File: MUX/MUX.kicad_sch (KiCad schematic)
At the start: 103 parts, among them P1 Conn_02x36_Top_Bottom, P2 DB9_Male, P3 DB9_Male, P4 DB9_Male, P5 DB9_Male

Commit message: WIP cards
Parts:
- added R16: 1K, symbol Device:R
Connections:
- net ~{ReadInput} is gone; now on net GND: U_B5.1 (OEa), U_B5.15 (OEb)
- net +5V: now also U_B2.14 (V_{CC}), R16.2; no longer U_B2.1 (V_{CC})
- net Data.InBD_{1}: now also U_H1.38 (CLS_{1}), U_H2.38 (CLS_{1}), U_H3.38 (CLS_{1})
- net GND: now also U_B2.7 (GND), U_C1.2 (Ia<b), U_C1.4 (Ia>b), U_C2.2 (Ia<b), U_C2.4 (Ia>b), U_C7.10 (CET), U_C7.9 (~{PE}); no longer U_B2.8 (GND)
- net ~{Reset}: now also U_C8.13
- net Write: now reaches U_B4.4, U_D2.12
- net Write: now also U_D1.2
- net INT_Pending: now reaches U_B7.9, U_E7.11
- net INT_Pending: now also U_B7.5
- net SysA_{3}: now reaches U_A1.12, U_B1.12, U_D1.3, U_D1.4, U_D1.5, U_E4.20 (A3)
- net ~{INT_Request}: now reaches U_A3.10, U_A7.10, U_B7.6, U_D8.2 (D)
- net INT_Request: now reaches U_A3.4, U_A7.5, U_A7.8, U_B7.1
- net ForceTXEInt: now reaches U_C6.10, U_C6.4, U_D3.8, U_E7.1, U_E7.4
- net ~{SysDataOutEN}: now reaches U_A5.9 (OE), U_A6.9 (OE), U_A8.8
- net ~{DirectRead}: now reaches U_C6.2, U_D1.8, U_E2.12 (A3)
- net at U_C6.3: now also U_A8.9; no longer U_D8.1 (~{R})
- net INR_OUT: now reaches U_A4.10, U_A4.13, U_A4.2, U_A4.4, U_A7.3
- net ~{INT_INH}: now reaches U_B7.10
- net ~{INT_INH}: now also U_A3.9, U_A8.12, U_B7.4
- net LevelAllow: now reaches U_B7.13
- net LevelAllow: now also U_A3.5, U_B3.7 (Oa<b)
- net at U_C8.4, U_D8.5 (Q): now also U_C8.1
- net MUX3.RxD: now reaches U_F4.2 (I1), U_F5.8, U_F6.7 (D3)
- net Read: now reaches U_B4.2, U_D2.11, U_D3.3
- net Read: now also U_D1.9
- net at U_D2.13: now also U_D2.2
- net DirectAddressed: now reaches U_C1.6 (Oa=b), U_D1.1, U_D3.1
- net DirectAddressed: now also U_D1.11
- net ~{DirectAddressed}: now reaches U_D3.2
- net ~{DirectAddressed}: now also U_B6.1, U_D2.3
- net Phase3: now reaches U_C7.12 (Q2)
- net Phase3: now also U_D2.9
- net Phase2: now reaches U_C7.13 (Q1)
- net Phase2: now also U_C7.5 (D2)
- net Phase1: now reaches U_C7.14 (Q0), U_D1.13, U_J7.1
- net Phase1: now also U_C7.4 (D1)
- net at U_C7.3 (D0), U_C7.6 (D3): now also U_D8.1 (~{R}), R16.1
- net CommonRead: now reaches U_D2.4
- net CommonRead: now also U_D2.8, U_D3.5
- net ~{SelfReset}: now reaches U_A7.12, U_B6.13, U_B8.8 (~{Q})
- net ~{DirectWrite}: now reaches U_D1.12, U_E4.18 (E0), U_E4.19 (E1)
- net D4_1 renamed ~{CommonRead}
- net RTS_EN renamed RTS_REG_EN
- net ~{is_common_addressed} renamed ~{CommonAddressed}
- no-connect marks 82 -> 136
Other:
- note added: "(~{Reset})"
- note added: "(~{Set})"
- note added: "MUX0"
- note added: "Status registers only output 6 bits this drives the other 2 high bits to 0 (see U_D4)"
- note added: "The shift function isn't even used. lul This register holds the value for the custom baud rate select."
- note added: "This counter pair provides a divide-by-N Loading the register will reset both counters so do not change while send or receive is in progress These count UP so the formula will be: Baud = MaxBaud / (256 - N) N must be less than 255 or it will not count *MaxBaud = Crystal / 256"
- note added: "U_B2B matches the high nibble including ~{A_{15}} which on the CPU6, places the device in the 0x3Fnnn memory range for older buses, it's just 0xFnnn"
- note added: "congradulations! it's a shift register with reset! This provides the read/write cycle phases phase 1 is used to fetch data during write phase 3 will assert ~{DRDY} at cycle end"
- note added: "low register"
- note removed: "(via)"
- note removed: "15 or 14? (needs lookup)"
- note removed: "C7(input) to D2.9 (via)"
- note removed: "D2.8/D3.5(via)"
- note removed: "MUX4"
- note removed: "TODO"
- note removed: "The shift function isn't even used. lul"
- note removed: "This matches the high nibble including ~{A_{15}} which on the CPU6, places the device in the 0x3Fnnn memory range for older buses, it's just 0xFnnn"
- note removed: "addressed"
- note removed: "addressed (via)"
- note removed: "is read"
- note removed: "not high reg probably pin 10"
- note removed: "not write"
- note removed: "read"
- note removed: "to reset?"
- note removed: "what even is this thing? is it right?"
- note removed: "write"
- note removed: "~{is addressed}"
- note removed: "~{read}"
- moved on the sheet: P2, P3, P4, P5, R1, R10, R13, R15, R2, R3, R4, R5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

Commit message: finished MUX
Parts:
- U_B2: symbol 74xx:SN7425 -> 74xx_legacy:SN7425
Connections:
- net RTS4_TTL is gone; now on net RTS3_TTL: U_K8.7 (Q3), U_LL8.3
- net RTS1_TTL: now also U_K8.5 (Q1), U_L8.3; no longer U_K8.4 (Q0), U_L8.2
- net RTS2_TTL: now also U_K8.6 (Q2), U_LL8.2; no longer U_K8.5 (Q1), U_L8.3
- net RTS3_TTL: no longer U_K8.6 (Q2), U_LL8.2
- net TX_{2}_TTL: now reaches U_K6.10, U_L6.3
- net ~{TX_{2}_EIA}: now reaches P4.7, U_K6.11, U_K6.12
- net SysA_{2}: now reaches U_A1.6, U_B1.1, U_E2.13 (A2), U_E4.21 (A2)
- net CausePending: now reaches U_B1.11, U_B8.4 (~{S}), U_D8.6 (~{Q})
- net SysA_{1}: now reaches U_A1.4, U_B1.2, U_B1.4, U_E2.14 (A1), U_E4.22 (A1)
- net SysA_{0}: now reaches U_A1.2, U_B1.3, U_E2.15 (A0), U_E4.23 (A0)
- net MMIO_HSel: now reaches U_B1.5, U_C1.3 (Ia=b), U_C2.6 (Oa=b)
- net CTS_{1}_TTL: now reaches U_F2.10 (I4), U_K6.2
- net LoadCR_{0}: now reaches U_E5.2, U_H1.34 (CRL), U_L1.13 (E01), U_L1.4 (E23)
- net TxBE_{3}: now reaches U_E3.11, U_E6.3 (C), U_F4.14 (I6)
- net RxD_{2}: now reaches U_F3.2 (I1), U_F5.6, U_F6.6 (D2)
- net TX_{2}_OUT: now reaches U_H3.25 (TxOUT), U_K6.13
- net ~{RTS_{3}}: now reaches P5.4, U_LL8.6
- net ~{RTS_{2}}: now reaches P4.4, U_LL8.7
- net LoadCR_{1}: now reaches U_E5.4, U_H2.34 (CRL), U_L2.13 (E01), U_L2.4 (E23)
- net ~{ReadSR_{0}}: now reaches U_E1.13, U_E2.1 (0), U_F1.1 (OEa), U_F1.15 (OEb)
- net ~{ReadRxB_{0}}: now reaches U_E2.2 (1), U_H1.18 (~{RxDR}), U_H1.4 (~{RxB_OE})
- net ~{ReadSR_{1}}: now reaches U_E1.12, U_E2.3 (2), U_F2.1 (OEa), U_F2.15 (OEb)
- net ~{ReadRxB_{1}: now reaches U_E2.4 (3), U_H2.18 (~{RxDR}), U_H2.4 (~{RxB_OE})
- net ~{ReadSR_{2}}: now reaches U_E1.10, U_E2.5 (4), U_F3.1 (OEa), U_F3.15 (OEb)
- net ~{ReadRxB_{2}}: now reaches U_E2.6 (5), U_H3.18 (~{RxDR}), U_H3.4 (~{RxB_OE})
- net ~{ReadSR_{3}: now reaches U_E1.9, U_E2.7 (6), U_F4.1 (OEa), U_F4.15 (OEb)
- net ~{ReadRxB_{3}}: now reaches U_E2.9 (7), U_H4.18 (~{RxDR}), U_H4.4 (~{RxB_OE})
- net ~{INTHandled}: now reaches U_C8.1, U_C8.4, U_D8.5 (Q)
- net RX_{3}_IN: now reaches U_H4.20 (RxIN), U_L7.10 (4Y)
- net RX_{2}_IN: now reaches U_H3.20 (RxIN), U_L7.12 (2Y)
- net ~{CTS_{2}}: now reaches P4.2, U_L7.4 (1A)
- net ~{RX_{2}}: now reaches P4.8, U_L7.5 (2A)
- net ~{CTS_{3}}: now reaches P5.2, U_L7.6 (3A)
- net ~{RX_{3}}: now reaches P5.8, U_L7.7 (4A)
- net CTS_{3}_TTL: now reaches U_F4.10 (I4), U_J6.2
- net FrameF_{3}: now reaches U_F4.12 (I5), U_H4.14 (FError)
- net ParityF_{3}: now reaches U_F4.4 (I2), U_H4.13 (PError)
- net OverrunF_{3}: now reaches U_F4.6 (I3), U_H4.15 (OError)
- net LoadCR_{2}: now reaches U_E5.6, U_H3.34 (CRL), U_L3.13 (E01), U_L3.4 (E23)
- net TxBE_{1}: now reaches U_D6.11 (C), U_E3.6, U_F2.14 (I6)
- net TX_{1}_TTL: now reaches U_K6.4, U_LL6.3
- net ~{TX_{1}}: now reaches P3.6, U_LL6.6
- net TX_{3}_OUT: now reaches U_H4.25 (TxOUT), U_J5.13
- net LoadCR_{3}: now reaches U_E5.10, U_H4.34 (CRL), U_L4.13 (E01), U_L4.4 (E23)
- net ~{CauseHold}: now reaches U_E7.8, U_F6.13 (E01), U_F6.4 (E23), U_F7.13 (E01), U_F7.4 (E23)
- net TX_{3}_TTL: now reaches U_J5.4, U_L6.2
- net ~{TX_{2}}: now reaches P4.6, U_L6.6
- net ~{TX_{3}}: now reaches P5.6, U_L6.7
- net CTS_{2}_TTL: now reaches U_F3.10 (I4), U_J6.12
- net ParityF_{1}: now reaches U_F2.4 (I2), U_H2.13 (PError)
- net FrameF_{1}: now reaches U_H2.14 (FError)
- net FrameF_{1}: now also U_F2.12 (I5)
- net OverrunF_{1}: now reaches U_H2.15 (OError)
- net OverrunF_{1}: now also U_F2.6 (I3)
- net RX_{1}_IN: now reaches U_H2.20 (RxIN), U_L5.10 (4Y)
- net TX_{1}_OUT: now reaches U_H2.25 (TxOUT), U_J6.3
- net ~{CREndStrobe}: now reaches U_B8.5 (Q), U_C8.12
- net ~{TX_{3}_EIA}: now reaches P5.7, U_J5.12, U_J5.3
- net ParityF_{2}: now reaches U_F3.4 (I2), U_H3.13 (PError)
- net FrameF_{2}: now reaches U_F3.12 (I5), U_H3.14 (FError)
- net OverrunF_{2}: now reaches U_F3.6 (I3), U_H3.15 (OError)
- net ~{CTS_{1}}: now reaches P3.2, U_L5.6 (3A)
- net ~{TX_{1}_EIA}: now reaches P3.7, U_J6.4, U_K6.3
- net ~{RX_{1}}: now reaches P3.8, U_L5.7 (4A)
- net CTS_{0}_TTL: now reaches U_F1.10 (I4), U_J5.10
- net FrameF_{0}: now reaches U_F1.12 (I5), U_H1.14 (FError)
- net TxBE_{0}: now reaches U_D6.3 (C), U_E3.3, U_F1.14 (I6)
- net ParityF_{0}: now reaches U_F1.4 (I2), U_H1.13 (PError)
- net OverrunF_{0}: now reaches U_F1.6 (I3), U_H1.15 (OError)
- net LoadIPL: now reaches U_C5.10 (CP), U_D3.12
- net RX_{0}_IN: now reaches U_H1.20 (RxIN), U_L5.12 (2Y)
- net TxBE_{2}: now reaches U_E3.8, U_E6.11 (C), U_F3.14 (I6)
- net CTS1 renamed ~{CTS_{0}}
- net F6_D0 renamed RxD_{0}
- net F6_D1 renamed RxD_{1}
- net MUX3.RxD renamed RxD_{3}
- net RTS1 renamed ~{RTS_{0}}
- net RTS2 renamed ~{RTS_{1}}
- net RTS_REG_EN renamed ~{RTS_REG_EN}
- net RXD1 renamed ~{RX_{0}}
- net TXD1 renamed ~{TX_{0}}
- net TXD1_BUF renamed TX_{0}_TTL
- net TXD1_TTL renamed TX_{0}_OUT
- net ~{CBRL} renamed ~{LoadCBR}
- net ~{CRL1} renamed ~{LoadCR_{0}}
- net ~{CRL2} renamed ~{LoadCR_{1}}
- net ~{CRL3} renamed ~{LoadCR_{2}}
- net ~{CRL4} renamed ~{LoadCR_{3}}
- net ~{IPLL} renamed ~{LoadIPL}
- net ~{RTSL} renamed ~{LoadRTS}
- net ~{TXBL1} renamed ~{LoadTxB_{0}}
- net ~{TXBL2} renamed ~{LoadTxB_{1}}
- net ~{TXBL3} renamed ~{LoadTxB_{2}}
- net ~{TXBL4} renamed ~{LoadTxB_{3}}
- net ~{TXD1_TTL} renamed ~{TX_{0}_EIA}
- new net RTS0_TTL: U_K8.4 (Q0), U_L8.2
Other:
- note added: "(-12V)"
- note added: "(GND)"
- note added: "*^{1} Reading this register is only valid during an interrupt"
- note added: "*^{2} Baud = Crystal / (256 * (256 - N)); N != 0"
- note added: "1.5"
- note added: "1200"
- note added: "19200"
- note added: "2400"
- note added: "300"
- note added: "4"
- note added: "4800"
- note added: "4915200 MHz"
- note added: "5"
- note added: "6"
- note added: "7"
- note added: "75"
- note added: "8"
- note added: "9"
- note added: "9600"
- note added: "A"
- note added: "B"
- note added: "Baud"
- note added: "Baud Rate Gen Divide *^{2}"
- note added: "Baud Rate Select"
- note added: "C"
- note added: "CTS"
- note added: "Card Address"
- note added: "Card Number"
- note added: "Clear to Send (pin 2)"
- note added: "Control Bits"
- note added: "D"
- note added: "D8A when set, will always set B8A"
- note added: "Data"
- note added: "Data Bits Length"
- note added: "E"
- note added: "Even"
- note added: "F"
- note added: "F20F *^{1}"
- note added: "Force TXE MUX 3..0"
- note added: "FrEr"
- note added: "Framing Error"
- note added: "Interrupt Cause MMIO bits (0xF20F Read)"
- note added: "Interrupts Off (Any write)"
- note added: "Interrupts On (Any write)"
- note added: "Length Select"
- note added: "MUX 0"
- note added: "MUX 1"
- note added: "MUX 2"
- note added: "MUX 3"
- note added: "MUX Card Reset (Any write)"
- note added: "N"
- note added: "N / 16"
- note added: "N / 2"
- note added: "N / 256"
- note added: "N / 4"
- note added: "N / 64"
- note added: "N / 8"
- note added: "N/A"
- note added: "OvRE"
- note added: "PDis"
- note added: "PEr"
- note added: "Parity 0=Enable, 1=Disable"
- note added: "Parity 0=Odd, 1=Even"
- note added: "Parity Mismatch Error"
- note added: "Q follows D when Enabled (H)"
- note added: "Rate Gen"
- note added: "Read"
- note added: "Receive Data Available"
- note added: "Receive Overrun"
- note added: "Reg"
- note added: "Rx Data"
- note added: "RxDi"
- note added: "Set IPL"
- note added: "Status Bits"
- note added: "Stop"
- note added: "Stop Bits Length"
- note added: "The shift function isn't even used. lul This register holds the value for the custom baud rate select. a 74LS273 might have been a better option"
- note added: "This counter pair provides a divide-by-N Loading the register will reset both counters this skews the output, so do not change while send or receive is in progress These count UP so the formula will be: Baud = MaxBaud / (256 - N) N must be less than 255 or it will not count *MaxBaud = Crystal / 256"
- note added: "Transmit Buffer Empty"
- note added: "Tx Data"
- note added: "TxEm"
- note added: "Write"
- note added: "fanout is at most 12 did they assume that the 8835 can't drive that?"
- note added: "it's a shift register with reset! This provides the read/write cycle phases phase 1 is used to fetch data during write phase 3 will assert ~{DRDY} at cycle end"
- note added: "this nand will go low when 0xF20F is accessed AND this device dispatched an interrupt"
- note removed: "A0"
- note removed: "A1"
- note removed: "A2"
- note removed: "A3"
- note removed: "E8"
- note removed: "E8 Func"
- note removed: "EN"
- note removed: "F8"
- note removed: "F8 Func"
- note removed: "I/O bits"
- note removed: "S0"
- note removed: "S1"
- note removed: "S2"
- note removed: "The shift function isn't even used. lul This register holds the value for the custom baud rate select."
- note removed: "This counter pair provides a divide-by-N Loading the register will reset both counters so do not change while send or receive is in progress These count UP so the formula will be: Baud = MaxBaud / (256 - N) N must be less than 255 or it will not count *MaxBaud = Crystal / 256"
- note removed: "congradulations! it's a shift register with reset! This provides the read/write cycle phases phase 1 is used to fetch data during write phase 3 will assert ~{DRDY} at cycle end"
- note removed: "ok"
- note removed: "ok via"
- note removed: "should connect data out? enable?"
- note removed: "should connect to buffer input"
- note removed: "this nand will go low when 0xF20F is accessed AND this device is interrupting AND interrupts are not preempted"
- note removed: "~{D5_En}"
- moved on the sheet: JP1, JP2, JP3, JP4, P2, P3, P4, P5, R1, R10, R11, R12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

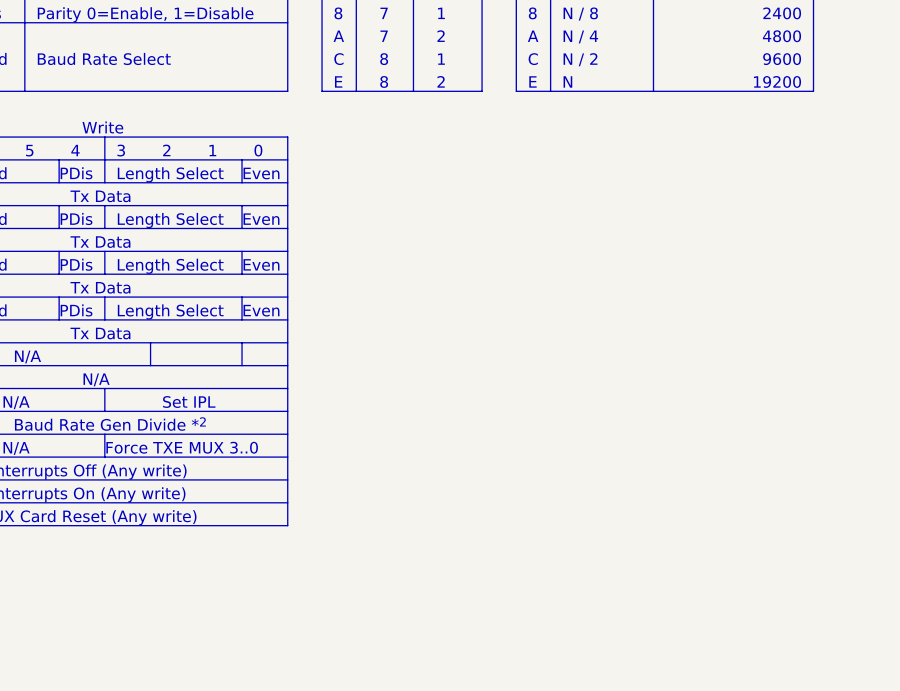
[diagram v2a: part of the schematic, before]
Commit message: MUX table, CPU net labels, partial DSK
MUX register table was missing description of RTS
Some internal nets in CPU were renamed to better describe them
DSK1 draft + DSK2 wip added
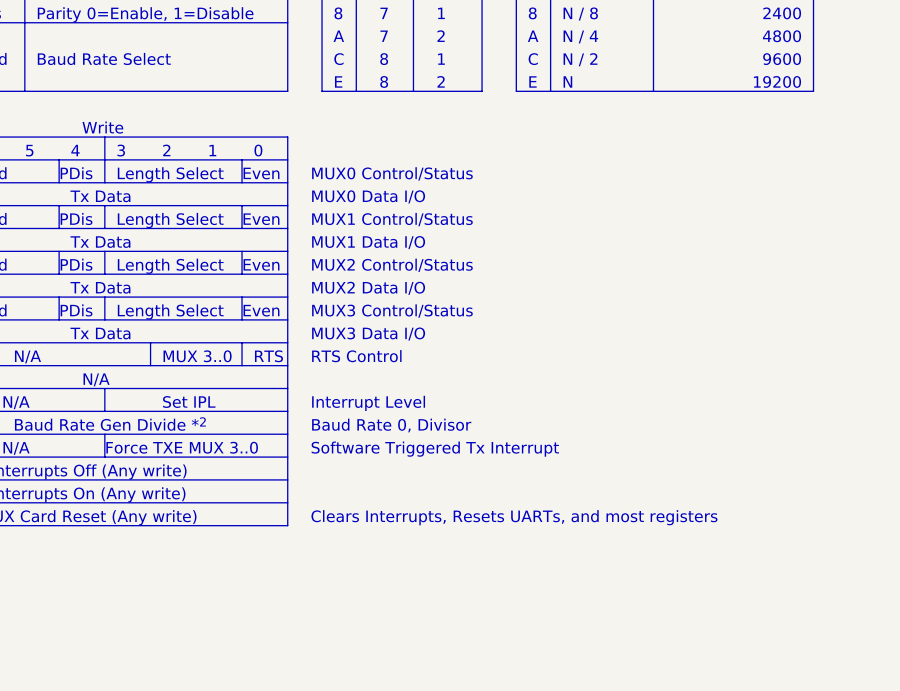
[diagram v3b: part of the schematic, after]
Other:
- note added: "Baud Rate 0, Divisor"
- note added: "Clears Interrupts, Resets UARTs, and most registers"
- note added: "Interrupt Level"
- note added: "MUX 3..0"
- note added: "MUX0 Control/Status"
- note added: "MUX0 Data I/O"
- note added: "MUX1 Control/Status"
- note added: "MUX1 Data I/O"
- note added: "MUX2 Control/Status"
- note added: "MUX2 Data I/O"
- note added: "MUX3 Control/Status"
- note added: "MUX3 Data I/O"
- note added: "RTS"
- note added: "RTS Control"
- note added: "Software Triggered Tx Interrupt"
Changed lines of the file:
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@@
     (stroke (width 0) (type default) (color 0 0 0 0))
   )
+  (text "MUX1 Data I/O" (at 948.69 435.61 0)
+    (effects (font (size 1.27 1.27)) (justify left bottom))
+  )
   (text "F" (at 902.97 466.09 0)
     (effects (font (size 1.27 1.27)) (justify left bottom))
@@
     (effects (font (size 1.27 1.27)) (justify left bottom))
   )
+  (text "MUX2 Data I/O" (at 948.69 440.69 0)
+    (effects (font (size 1.27 1.27)) (justify left bottom))
+  )
   (text "FrEr" (at 881.38 433.07 0)
     (effects (font (size 1.27 1.27)) (justify left bottom))
@@
   )
   (text "N / 256" (at 976.63 402.59 0)
+    (effects (font (size 1.27 1.27)) (justify left bottom))
+  )
+  (text "Clears Interrupts, Resets UARTs, and most registers"
+    (at 948.69 466.09 0)
     (effects (font (size 1.27 1.27)) (justify left bottom))
   )
@@
     (effects (font (size 1.27 1.27)) (justify left bottom))
   )
+  (text "MUX0 Data I/O" (at 948.69 430.53 0)
+    (effects (font (size 1.27 1.27)) (justify left bottom))
+  )
   (text "4" (at 862.33 410.21 0)
     (effects (font (size 1.27 1.27)) (justify left bottom))
@@
   )
   (text "0" (at 951.23 400.05 0)
+    (effects (font (size 1.27 1.27)) (justify left bottom))
+  )
+  (text "MUX3 Data I/O" (at 948.69 445.77 0)
     (effects (font (size 1.27 1.27)) (justify left bottom))
   )
@@
     (effects (font (size 1.27 1.27)) (justify left bottom))
   )
+  (text "MUX 3..0" (at 932.18 448.31 0)
+    (effects (font (size 1.27 1.27)) (justify left bottom))
+  )
   (text "OvRE" (at 876.3 438.15 0)
     (effects (font (size 1.27 1.27)) (justify left bottom))
@@
     (effects (font (size 1.27 1.27)) (justify left bottom))
   )
+  (text "RTS Control" (at 948.69 448.31 0)
+    (effects (font (size 1.27 1.27)) (justify left bottom))
+  )
   (text "RxDi" (at 896.62 433.07 0)
     (effects (font (size 1.27 1.27)) (justify left bottom))
@@
     (effects (font (size 1.27 1.27)) (justify left bottom))
   )
+  (text "RTS" (at 942.34 448.31 0)
+    (effects (font (size 1.27 1.27)) (justify left bottom))
+  )
   (text "Set IPL" (at 932.18 453.39 0)
     (effects (font (size 1.27 1.27)) (justify left bottom))
@@
     (effects (font (size 1.27 1.27)) (justify left bottom))
   )
+  (text "MUX2 Control/Status" (at 948.69 438.15 0)
+    (effects (font (size 1.27 1.27)) (justify left bottom))
+  )
+  (text "MUX1 Control/Status" (at 948.69 433.07 0)
+    (effects (font (size 1.27 1.27)) (justify left bottom))
+  )
   (text "FrEr" (at 866.14 407.67 0)
     (effects (font (size 1.27 1.27)) (justify left bottom))
@@
   )
   (text "3" (at 902.97 435.61 0)
+    (effects (font (size 1.27 1.27)) (justify left bottom))
+  )
+  (text "MUX3 Control/Status" (at 948.69 443.23 0)
     (effects (font (size 1.27 1.27)) (justify left bottom))
   )
@@
     (effects (font (size 1.27 1.27)) (justify left bottom))
   )
+  (text "Software Triggered Tx Interrupt" (at 948.69 458.47 0)
+    (effects (font (size 1.27 1.27)) (justify left bottom))
+  )
   (text "Status registers only output 6 bits\nthis drives the other 2 high bits to 0\n(see U_D4)"
     (at 292.1 436.88 0)
     (effects (font (size 1.27 1.27)) (justify left bottom))
   )
+  (text "MUX0 Control/Status" (at 948.69 427.99 0)
+    (effects (font (size 1.27 1.27)) (justify left bottom))
+  )
   (text "6" (at 906.78 415.29 0)
     (effects (font (size 1.27 1.27)) (justify left bottom))
@@
     (effects (font (size 1.27 1.27)) (justify left bottom))
   )
+  (text "Baud Rate 0, Divisor" (at 948.69 455.93 0)
+    (effects (font (size 1.27 1.27)) (justify left bottom))
+  )
   (text "Stop Bits Length" (at 918.21 402.59 0)
     (effects (font (size 1.27 1.27)) (justify left bottom))
@@
     (effects (font (size 1.27 1.27)) (justify left bottom))
   )
+  (text "Interrupt Level" (at 948.69 453.39 0)
+    (effects (font (size 1.27 1.27)) (justify left bottom))
+  )

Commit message: misc readability, fix MUX errata
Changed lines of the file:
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@@
   (title_block
     (title "Centurion - 4 Port MUX (Serial Multiplex) Card")
-    (date "2022-09-25")
-    (rev "1.1")
+    (date "2023-05-03")
+    (rev "1.2")
     (company "Meisaka Yukara")
     (comment 1 "Visually Reverse Engineered")
@@
     (stroke (width 0) (type default) (color 0 0 0 0))
   )
-  (polyline (pts (xy 946.15 402.59) (xy 905.51 402.59))
+  (polyline (pts (xy 946.15 405.13) (xy 905.51 405.13))
     (stroke (width 0) (type solid) (color 0 0 0 0))
   )
@@
     (effects (font (size 1.27 1.27)) (justify left bottom))
   )
-  (text "C" (at 951.23 415.29 0)
+  (text "6" (at 951.23 415.29 0)
     (effects (font (size 1.27 1.27)) (justify left bottom))
   )
@@
     (effects (font (size 1.27 1.27)) (justify left bottom))
   )
-  (text "8" (at 951.23 410.21 0)
+  (text "4" (at 951.23 410.21 0)
     (effects (font (size 1.27 1.27)) (justify left bottom))
   )
@@
     (effects (font (size 1.27 1.27)) (justify left bottom))
   )
-  (text "6" (at 951.23 407.67 0)
+  (text "A" (at 951.23 407.67 0)
     (effects (font (size 1.27 1.27)) (justify left bottom))
   )
@@
     (effects (font (size 1.27 1.27)) (justify left bottom))
   )
-  (text "Data Bits Length" (at 918.21 406.4 0)
+  (text "Data Bits Length" (at 918.21 403.86 0)
     (effects (font (size 1.27 1.27)) (justify left bottom))
   )
@@
     (effects (font (size 1.27 1.27)) (justify left bottom))
   )
-  (text "2" (at 951.23 402.59 0)
+  (text "8" (at 951.23 402.59 0)
     (effects (font (size 1.27 1.27)) (justify left bottom))
   )
@@
     (effects (font (size 1.27 1.27)) (justify left bottom))
   )
-  (text "4" (at 951.23 405.13 0)
+  (text "2" (at 951.23 405.13 0)
     (effects (font (size 1.27 1.27)) (justify left bottom))
   )
-  (text "A" (at 951.23 412.75 0)
+  (text "C" (at 951.23 412.75 0)
     (effects (font (size 1.27 1.27)) (justify left bottom))
   )
@@
     (effects (font (size 1.27 1.27)) (justify left bottom))
   )
-  (text "Stop Bits Length" (at 918.21 402.59 0)
+  (text "Stop Bits Length" (at 918.21 407.67 0)
     (effects (font (size 1.27 1.27)) (justify left bottom))
   )
